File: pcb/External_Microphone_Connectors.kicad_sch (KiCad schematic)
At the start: 36 parts, among them J11 Conn_01x04_Pin, J12 Conn_01x04_Pin, J20 Conn_01x04_Pin, J9 Conn_01x04_Pin, U5 AD8426ACPZ-R7, U6 AD8426ACPZ-R7

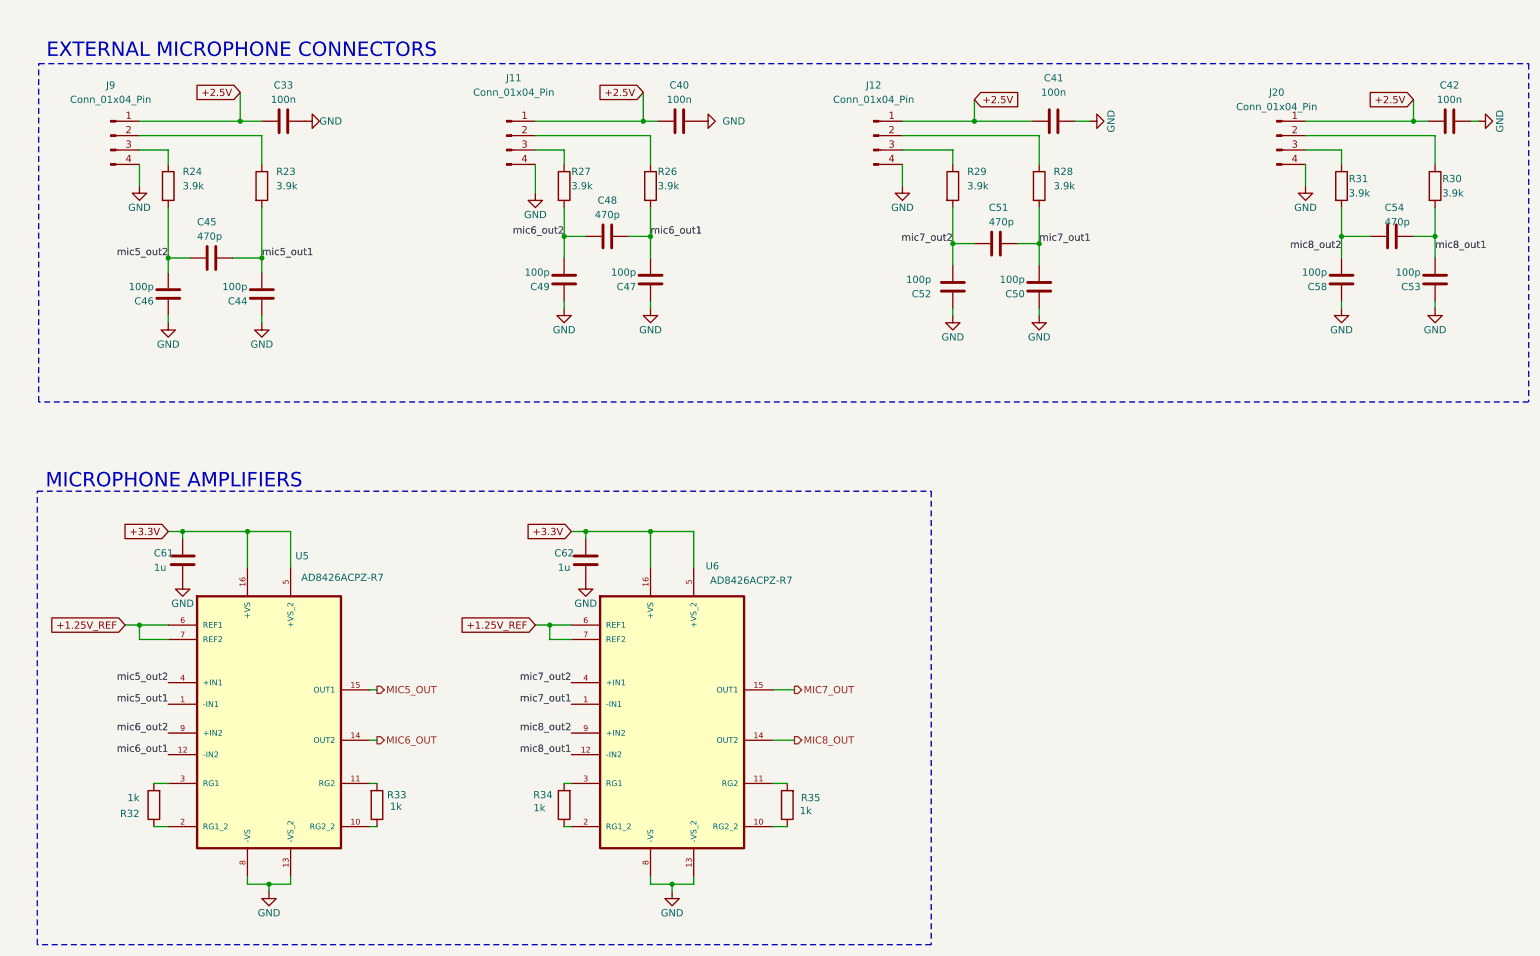
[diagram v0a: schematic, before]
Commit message: pcb: New PCB revision (#88)
- Rearrange schematics
- Better symbols and footprints
- Better names and graphics
- Add simulations for DC offset after AC coupling
- Add BOM
- Redraw PCB layout
- Proper position for pressure and humidity sensor
- Better positions for EXT headers
- Silkscreen text labels for headers, pins, mics, etc.
- Change supply polarity and pin numbers of ADA4511
- Change cap of switches to 100n to reduce BOM
- Change supply of sensors to unison 3.3V
- Rearrange ADC pins
- Add digital switches instead of manual headers
- Add logos

---------

Co-authored-by: oberfeli <felix.ober@mailbox.org>
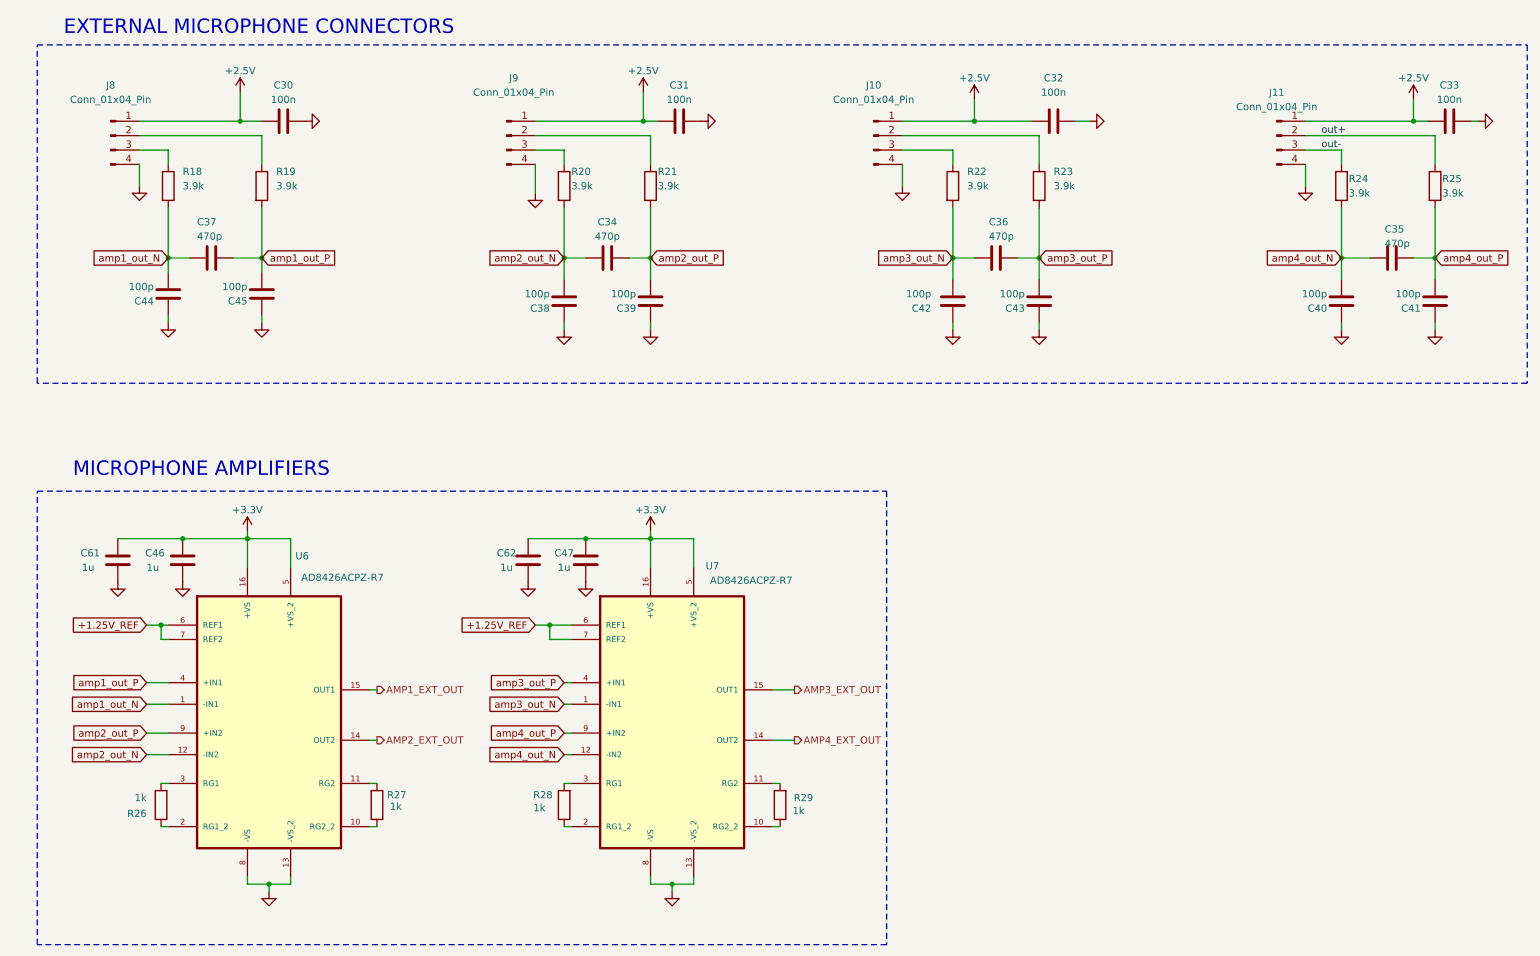
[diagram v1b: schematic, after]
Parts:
- added C61, C62: 1u, Capacitor_SMD:C_0603_1608Metric, symbol SensEdu:C
- C30: renamed from C33; footprint Capacitor_SMD:C_0805_2012Metric -> Capacitor_SMD:C_0603_1608Metric; symbol Device:C -> SensEdu:C
- C31: renamed from C40; footprint Capacitor_SMD:C_0805_2012Metric -> Capacitor_SMD:C_0603_1608Metric; symbol Device:C -> SensEdu:C
- C32: renamed from C41; footprint Capacitor_SMD:C_0805_2012Metric -> Capacitor_SMD:C_0603_1608Metric; symbol Device:C -> SensEdu:C
- C33: renamed from C42; footprint Capacitor_SMD:C_0805_2012Metric -> Capacitor_SMD:C_0603_1608Metric; symbol Device:C -> SensEdu:C
- C34: renamed from C48; footprint Capacitor_SMD:C_0805_2012Metric -> Capacitor_SMD:C_0603_1608Metric; symbol Device:C -> SensEdu:C
- C35: renamed from C54; footprint Capacitor_SMD:C_0805_2012Metric -> Capacitor_SMD:C_0603_1608Metric; symbol Device:C -> SensEdu:C
- C36: renamed from C51; footprint Capacitor_SMD:C_0805_2012Metric -> Capacitor_SMD:C_0603_1608Metric; symbol Device:C -> SensEdu:C
- C37: renamed from C45; footprint Capacitor_SMD:C_0805_2012Metric -> Capacitor_SMD:C_0603_1608Metric; symbol Device:C -> SensEdu:C
- C38: renamed from C49; footprint Capacitor_SMD:C_0805_2012Metric -> Capacitor_SMD:C_0603_1608Metric; symbol Device:C -> SensEdu:C
- C39: renamed from C47; footprint Capacitor_SMD:C_0805_2012Metric -> Capacitor_SMD:C_0603_1608Metric; symbol Device:C -> SensEdu:C
- C40: renamed from C58; footprint Capacitor_SMD:C_0805_2012Metric -> Capacitor_SMD:C_0603_1608Metric; symbol Device:C -> SensEdu:C
- C41: renamed from C53; footprint Capacitor_SMD:C_0805_2012Metric -> Capacitor_SMD:C_0603_1608Metric; symbol Device:C -> SensEdu:C
- C42: renamed from C52; footprint Capacitor_SMD:C_0805_2012Metric -> Capacitor_SMD:C_0603_1608Metric; symbol Device:C -> SensEdu:C
- C43: renamed from C50; footprint Capacitor_SMD:C_0805_2012Metric -> Capacitor_SMD:C_0603_1608Metric; symbol Device:C -> SensEdu:C
- C44: renamed from C46; footprint Capacitor_SMD:C_0805_2012Metric -> Capacitor_SMD:C_0603_1608Metric; symbol Device:C -> SensEdu:C
- C45: renamed from C44; footprint Capacitor_SMD:C_0805_2012Metric -> Capacitor_SMD:C_0603_1608Metric; symbol Device:C -> SensEdu:C
- C46: renamed from C61; footprint Capacitor_SMD:C_0805_2012Metric -> Capacitor_SMD:C_0603_1608Metric; symbol Device:C -> SensEdu:C
- C47: renamed from C62; footprint Capacitor_SMD:C_0805_2012Metric -> Capacitor_SMD:C_0603_1608Metric; symbol Device:C -> SensEdu:C
- J10: renamed from J12; symbol Connector:Conn_01x04_Pin -> SensEdu:Conn_01x04_Pin
- J11: renamed from J20; symbol Connector:Conn_01x04_Pin -> SensEdu:Conn_01x04_Pin
- J8: renamed from J9; symbol Connector:Conn_01x04_Pin -> SensEdu:Conn_01x04_Pin
- J9: renamed from J11; symbol Connector:Conn_01x04_Pin -> SensEdu:Conn_01x04_Pin
- R18: renamed from R24; footprint Resistor_SMD:R_0805_2012Metric -> Resistor_SMD:R_0603_1608Metric; symbol Device:R -> SensEdu:R
- R19: renamed from R23; footprint Resistor_SMD:R_0805_2012Metric -> Resistor_SMD:R_0603_1608Metric; symbol Device:R -> SensEdu:R
- R20: renamed from R27; footprint Resistor_SMD:R_0805_2012Metric -> Resistor_SMD:R_0603_1608Metric; symbol Device:R -> SensEdu:R
- R21: renamed from R26; footprint Resistor_SMD:R_0805_2012Metric -> Resistor_SMD:R_0603_1608Metric; symbol Device:R -> SensEdu:R
- R22: renamed from R29; footprint Resistor_SMD:R_0805_2012Metric -> Resistor_SMD:R_0603_1608Metric; symbol Device:R -> SensEdu:R
- R23: renamed from R28; footprint Resistor_SMD:R_0805_2012Metric -> Resistor_SMD:R_0603_1608Metric; symbol Device:R -> SensEdu:R
- R24: renamed from R31; footprint Resistor_SMD:R_0805_2012Metric -> Resistor_SMD:R_0603_1608Metric; symbol Device:R -> SensEdu:R
- R25: renamed from R30; footprint Resistor_SMD:R_0805_2012Metric -> Resistor_SMD:R_0603_1608Metric; symbol Device:R -> SensEdu:R
- R26: renamed from R32; footprint Resistor_SMD:R_0805_2012Metric -> Resistor_SMD:R_0603_1608Metric; symbol Device:R -> SensEdu:R
- R27: renamed from R33; footprint Resistor_SMD:R_0805_2012Metric -> Resistor_SMD:R_0603_1608Metric; symbol Device:R -> SensEdu:R
- R28: renamed from R34; footprint Resistor_SMD:R_0805_2012Metric -> Resistor_SMD:R_0603_1608Metric; symbol Device:R -> SensEdu:R
- R29: renamed from R35; footprint Resistor_SMD:R_0805_2012Metric -> Resistor_SMD:R_0603_1608Metric; symbol Device:R -> SensEdu:R
- U6: renamed from U5; symbol SensEdu:AD8426ACPZ-R7 -> SensEdu:AD8426ACPZ-R7_1
- renumbered U6 to U7
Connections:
- net +3.3V: now also C61.1, C62.1
- net GND: now also C61.2, C62.2
- net out+: now reaches J11.2 (Pin_2), R25.1
- net out-: now reaches J11.3 (Pin_3), R24.1
- net MIC5_OUT renamed AMP1_EXT_OUT
- net MIC6_OUT renamed AMP2_EXT_OUT
- net MIC7_OUT renamed AMP3_EXT_OUT
- net MIC8_OUT renamed AMP4_EXT_OUT
- net mic5_out1 renamed amp1_out_P
- net amp1_out_P: now also U6.4 (+IN1); no longer U6.1 (-IN1)
- net mic5_out2 renamed amp1_out_N
- net amp1_out_N: now also U6.1 (-IN1); no longer U6.4 (+IN1)
- net mic6_out1 renamed amp2_out_P
- net amp2_out_P: now also U6.9 (+IN2); no longer U6.12 (-IN2)
- net mic6_out2 renamed amp2_out_N
- net amp2_out_N: now also U6.12 (-IN2); no longer U6.9 (+IN2)
- net mic7_out1 renamed amp3_out_P
- net amp3_out_P: now also U7.4 (+IN1); no longer U7.1 (-IN1)
- net mic7_out2 renamed amp3_out_N
- net amp3_out_N: now also U7.1 (-IN1); no longer U7.4 (+IN1)
- net mic8_out1 renamed amp4_out_P
- net amp4_out_P: now also U7.9 (+IN2); no longer U7.12 (-IN2)
- net mic8_out2 renamed amp4_out_N
- net amp4_out_N: now also U7.12 (-IN2); no longer U7.9 (+IN2)
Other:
- title: SensEdu 0.7 -> SensEdu
- moved on the sheet: C34, C35, C36, C38, C39, C40, C41, C42, C43, R26, R29
